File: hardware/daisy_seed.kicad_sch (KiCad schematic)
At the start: 22 parts, among them J2 GPIO Header, J3 Micro_SD_Card, U3 Daisy_Seed, U4 H11L1SM

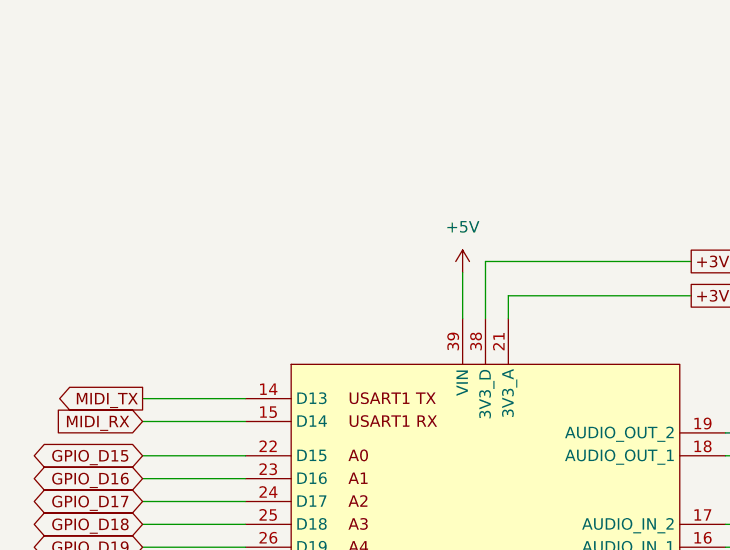
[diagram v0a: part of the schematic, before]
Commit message: cleanup - remove unused schematics
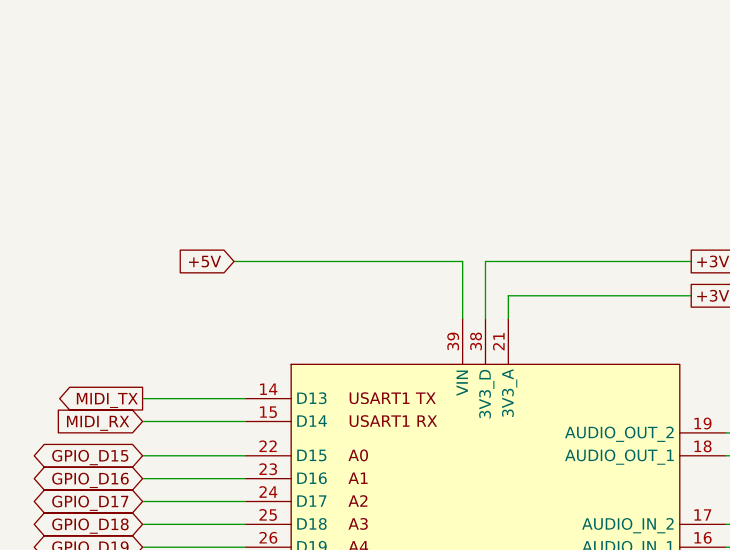
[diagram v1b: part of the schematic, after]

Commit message: wip
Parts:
- removed J_MIDI_IN1, J_MIDI_OUT1, J_MIDI_THRU1: DIN-5_180degree, symbol Connector:DIN-5_180degree
- added J_MIDI_IN1, J_MIDI_OUT1, J_MIDI_THRU1: SDS-50J, SDS50J, symbol SDS-50J:SDS-50J
- D2: value 1N4148WS -> 1N4148W; footprint Diode_SMD:D_SOD-323 -> Diode_SMD:D_SOD-123
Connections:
- net GND: now also R13.1, J_MIDI_IN1.2, J_MIDI_OUT1.2, J_MIDI_OUT1.5, J_MIDI_THRU1.2
- net at R14.2: now also J_MIDI_IN1.4
- net at R18.2: now also J_MIDI_THRU1.5
- net at R17.2: now also J_MIDI_THRU1.4
- net at R12.2: now also J_MIDI_OUT1.4
- net at R15.2: now also J_MIDI_IN1.5
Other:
- moved on the sheet: R13

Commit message: PCB Assembledish Design checks next
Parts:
- removed R_STAR1: 0R, Resistor_THT:R_Axial_DIN0207_L6.3mm_D2.5mm_P5.08mm_Vertical, symbol Device:R
- J3: footprint (none) -> Connector_Card:microSD_HC_Hirose_DM3AT-SF-PEJM5
- J_MIDI_IN_1: renamed from J_MIDI_IN1; footprint SDS50J -> libs:SDS50J
- J_MIDI_OUT_1: renamed from J_MIDI_OUT1; footprint SDS50J -> libs:SDS50J
- J_MIDI_THRU1: footprint SDS50J -> libs:SDS50J
- U3: footprint Daisy-Boards:DAISY_SEED_SMT -> daisy:DAISY_SEED_SMT
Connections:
- net GNDA is gone; now on net GND: U3.20 (AGND)
- net GND: now also J3.10 (Detect), J3.11 (SHIELD), J_MIDI_IN_1.MH1, J_MIDI_IN_1.MH2, J_MIDI_IN_1.MH3, J_MIDI_IN_1.MH4, J_MIDI_OUT_1.MH1, J_MIDI_OUT_1.MH2, J_MIDI_OUT_1.MH3, J_MIDI_OUT_1.MH4, J_MIDI_THRU1.MH1, J_MIDI_THRU1.MH2, J_MIDI_THRU1.MH3, J_MIDI_THRU1.MH4; no longer J_MIDI_OUT_1.5, R13.1
- net GPIO_D0: now also J2.1 (Pin_1); no longer J2.13 (Pin_13)
- net GPIO_D10: now also J2.9 (Pin_9); no longer J2.5 (Pin_5)
- net GPIO_D11: now also J2.11 (Pin_11); no longer J2.3 (Pin_3)
- net GPIO_D12: now also J2.13 (Pin_13); no longer J2.1 (Pin_1)
- net GPIO_D7: now also J2.3 (Pin_3); no longer J2.11 (Pin_11)
- net GPIO_D8: now also J2.5 (Pin_5); no longer J2.9 (Pin_9)
- new net: J_MIDI_OUT_1.5, R13.1
- no-connect marks 0 -> 6
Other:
- note removed: "Star ground: single-point AGND↔DGND connection"
